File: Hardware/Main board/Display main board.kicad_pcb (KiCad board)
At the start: 2 copper layers, 142.2 x 91.4 mm, 87 parts, among them J1 Board to Board, J2 BATT JST, J3 Conn_ARM_SWD_TagConnect_TC203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, P1 USB_C_Plug_USB2.0, SW1 USB BOOT, U1 BQ25895, U10 ABM8-272-T3, U2 W25Q32JVSS, U3 TS3USB221A, U4 AP7361C-33E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

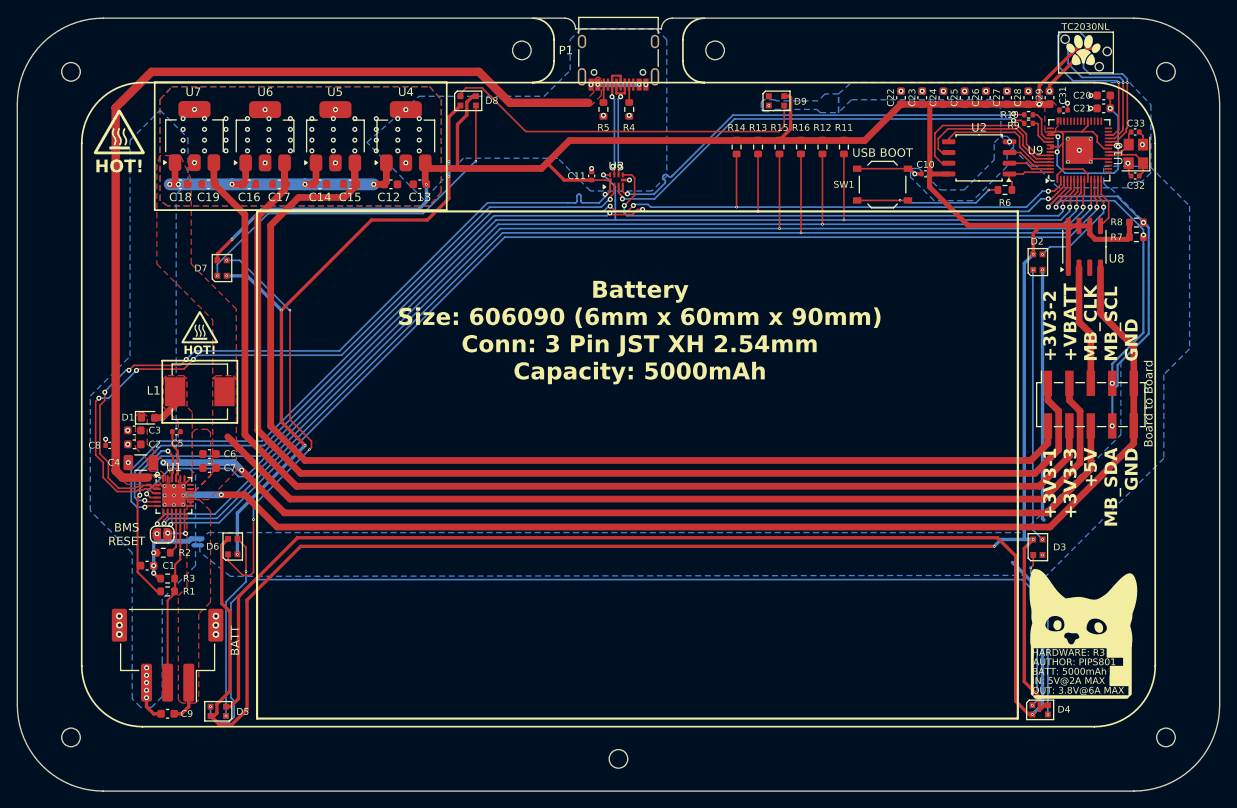
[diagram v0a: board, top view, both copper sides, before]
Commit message: move debug header
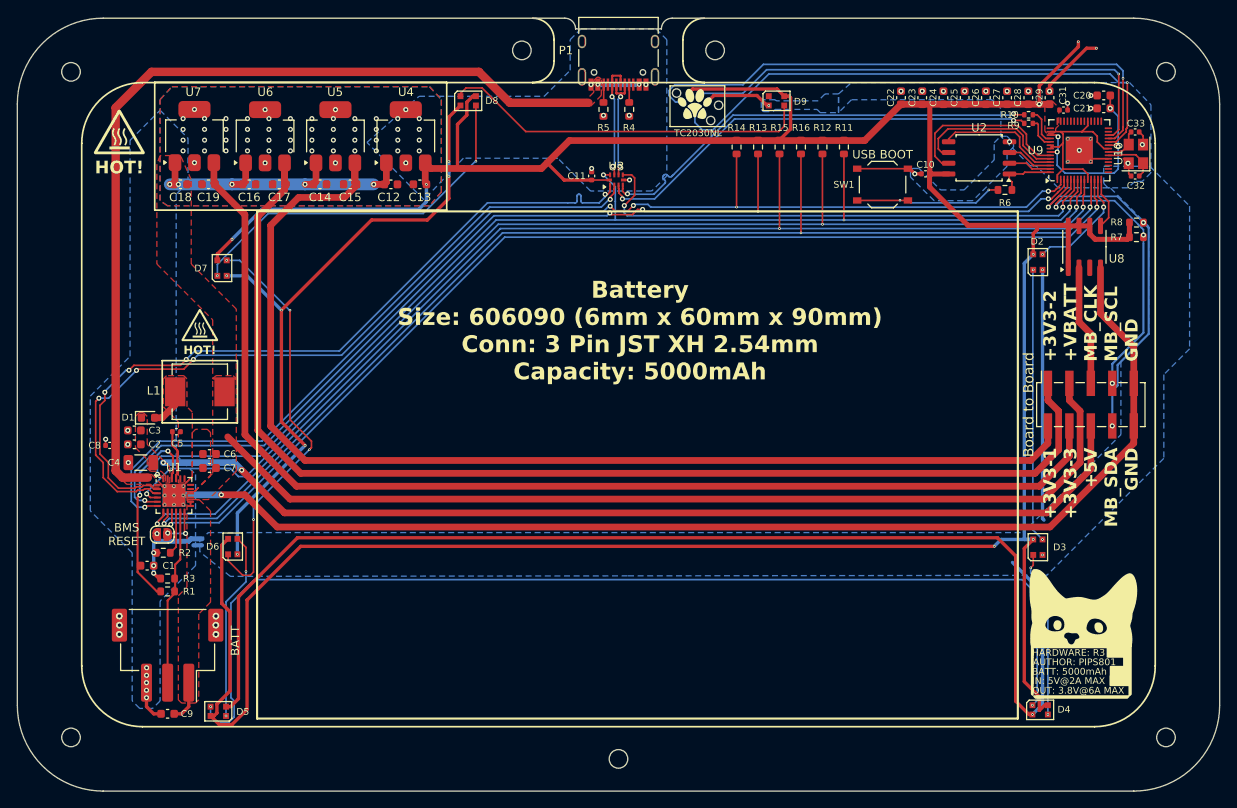
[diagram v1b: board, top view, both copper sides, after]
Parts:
- removed the G*** at (137.3, 96.5)
- moved J3 46.4 mm to (146.5, 61.3)
- moved G** 46.4 mm to (146.2, 60.9)
- moved G*** 0.25 mm to (87.6, 84.5)
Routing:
- net /RP2040/SWDIO: track 17.3 -> 67.0 mm
- net /RP2040/SWCLK: track 15.9 -> 63.9 mm
- net /RP2040/RUN: track 23.0 -> 59.1 mm
- net +3.3V: track 410.5 -> 422.2 mm, vias 7 -> 8
- net AGND: track 295.8 -> 303.8 mm, vias 31 -> 32

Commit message: Silkscreen sectioning
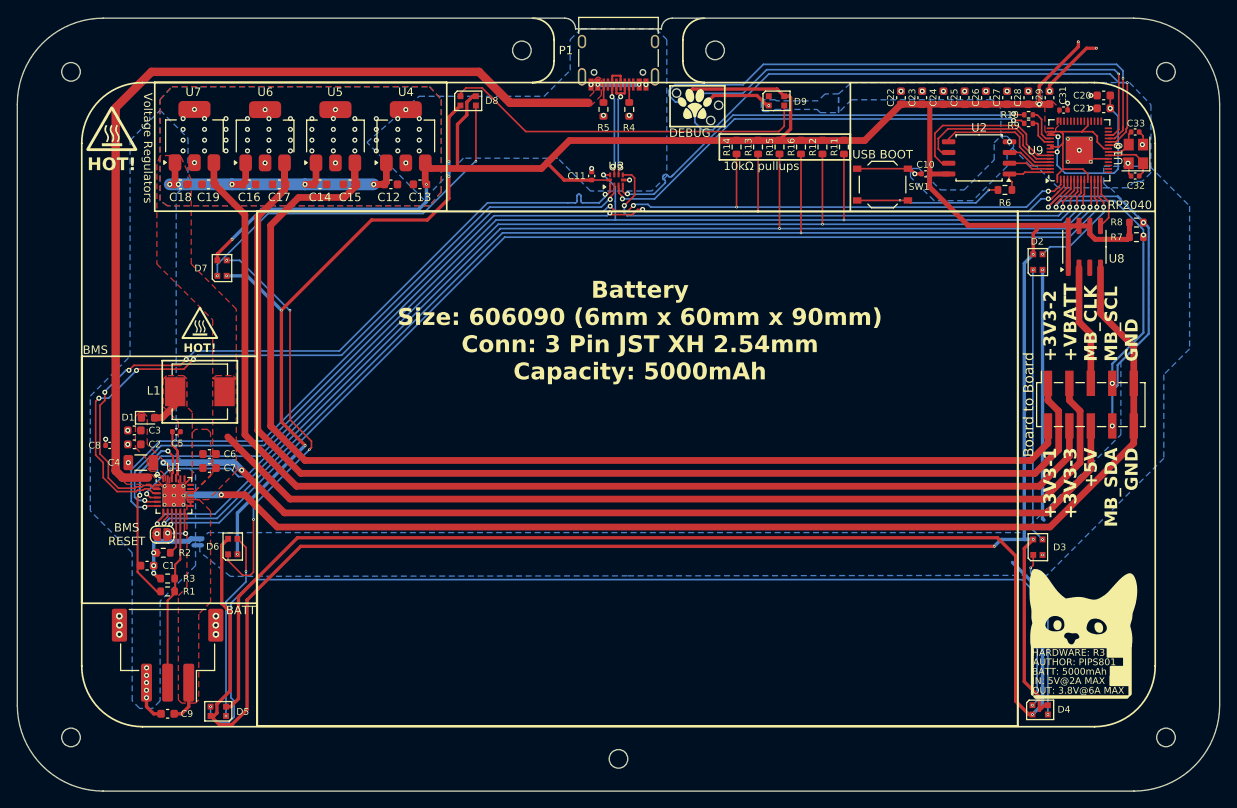
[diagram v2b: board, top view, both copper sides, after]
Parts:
- moved G*** 0.97 mm to (77.2, 61.2)
- moved G*** 0.25 mm to (87.6, 84.2)
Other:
- board text added: "10kΩ pullups"
- board text added: "BMS"
- board text added: "RP2040"
- board text added: "Voltage Regulators"
- board text removed: "TC2030NL"
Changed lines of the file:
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@@
 		(tags "resistor")
 		(property "Reference" "R13"
-			(at -2.286 0 180)
+			(at 0 1.143 -90)
 			(layer "F.SilkS")
 			(effects
@@
 		(tags "resistor")
 		(property "Reference" "R11"
-			(at -2.286 0 0)
+			(at 0 1.143 90)
 			(layer "F.SilkS")
 			(effects
@@
 		(tags "resistor")
 		(property "Reference" "R12"
-			(at -2.286 0 180)
+			(at 0 1.143 -90)
 			(layer "F.SilkS")
 			(effects
@@
 	(footprint "LOGO"
 		(layer "F.Cu")
-		(at 87.630001 84.464661)
+		(at 87.630001 84.210661)
 		(property "Reference" "G***"
 			(at 0 0 0)
@@
 		(tags "resistor")
 		(property "Reference" "R15"
-			(at -2.286 0 180)
+			(at 0 1.143 -90)
 			(layer "F.SilkS")
 			(effects
@@
 		(tags "resistor")
 		(property "Reference" "R16"
-			(at -2.286 0 180)
+			(at 0 1.143 -90)
 			(layer "F.SilkS")
 			(effects
@@
 		(tags "resistor")
 		(property "Reference" "R14"
-			(at -2.286 0 180)
+			(at 0 1.143 -90)
 			(layer "F.SilkS")
 			(effects
@@
 		(tags "SPST Tactile Switch")
 		(property "Reference" "SW1"
-			(at 4.572 0 360)
+			(at -4.318 -0.254 360)
 			(layer "F.SilkS")
 			(effects
@@
 	(footprint "LOGO"
 		(layer "F.Cu")
-		(at 78.105001 61.616062)
+		(at 77.216001 61.235062)
 		(property "Reference" "G***"
 			(at 0 0 0)
@@
 	(gr_rect
 		(start 82.296 58.395)
-		(end 116.84 73.508)
+		(end 116.84 73.635)
 		(stroke
 			(width 0.2)
@@
 		(layer "F.SilkS")
 	)
+	(gr_line
+		(start 184.404 73.66)
+		(end 200.66 73.66)
+		(stroke
+			(width 0.2)
+			(type default)
+		)
+		(layer "F.SilkS")
+	)
 	(gr_arc
 		(start 80.844 134.62)
@@
 		(layer "F.SilkS")
 	)
+	(gr_rect
+		(start 73.66 90.805)
+		(end 94.361 120.015)
+		(stroke
+			(width 0.2)
+			(type default)
+		)
+		(fill none)
+		(layer "F.SilkS")
+	)
 	(gr_line
 		(start 193.476 134.62)
@@
 		(end 149.733 63.627)
 		(stroke
-			(width 0.15)
+			(width 0.2)
 			(type default)
 		)
@@
 	(gr_rect
 		(start 94.404 73.66)
-		(end 184.404 133.66)
+		(end 184.404 134.549)
 		(stroke
 			(width 0.25)
@@
 	)
 	(gr_line
+		(start 200.66 73.66)
+		(end 200.66 65.604)
+		(stroke
+			(width 0.1)
+			(type default)
+		)
+		(layer "F.SilkS")
+	)
+	(gr_line
 		(start 144.78 53.34)
 		(end 144.78 55.88)
@@
 		(layer "F.SilkS")
 	)
+	(gr_rect
+		(start 149.098 64.516)
+		(end 164.592 67.564)
+		(stroke
+			(width 0.2)
+			(type default)
+		)
+		(fill none)
+		(layer "F.SilkS")
+	)
 	(gr_arc
 		(start 200.66 127.436)
@@
 		(layer "F.SilkS")
 	)
+	(gr_line
+		(start 164.592 73.66)
+		(end 164.592 58.42)
+		(stroke
+			(width 0.2)
+			(type default)
+		)
+		(layer "F.SilkS")
+	)
 	(gr_rect
 		(start 94.404 73.66)
@@
 		)
 	)
+	(gr_text "10kΩ pullups"
+		(at 154.06662 68.885664 0)
+		(layer "F.SilkS" knockout)
+		(effects
+			(font
+				(size 1 1)
+				(thickness 0.2)
+			)
+			(justify bottom)
+		)
+	)
 	(gr_text "BATT: 5000mAh"
 		(at 186.067629 128.566566 0)
@@
 	)
 	(gr_text "BATT\n"
-		(at 91.821 126.238 90)
-		(layer "F.SilkS")
+		(at 90.715641 120.8507 0)
+		(layer "F.SilkS" knockout)
 		(effects
 			(font
 				(size 1 1)
-				(thickness 0.15)
+				(thickness 0.2)
 			)
 			(justify left)
@@
 		)
 	)
-	(gr_text "TC2030NL"
-		(at 146.558 64.389 -0)
-		(layer "F.SilkS")
+	(gr_text "DEBUG"
+		(at 145.597381 64.380029 -0)
+		(layer "F.SilkS" knockout)
 		(effects
 			(font
-				(size 0.8 0.8)
-				(thickness 0.15)
+				(size 1 1)
+				(thickness 0.2)
+			)
+		)
+	)
+	(gr_text "RP2040"
+		(at 197.649945 73.492659 0)
+		(layer "F.SilkS" knockout)
+		(effects
+			(font
+				(size 1 1)
+				(thickness 0.2)
+			)
+			(justify bottom)
+		)
+	)
+	(gr_text "BMS"
+		(at 75.267646 90.637849 0)
+		(layer "F.SilkS" knockout)
+		(effects
+			(font
+				(size 1 1)
+				(thickness 0.2)
 			)
+			(justify bottom)
 		)
 	)
@@
 		)
 	)
+	(gr_text "Voltage Regulators"
+		(at 80.899 66.167 -90)
+		(layer "F.SilkS" knockout)
+		(effects
+			(font
+				(size 1 1)
+				(thickness 0.2)
+			)
+			(justify bottom)
+		)
+	)
 	(gr_text "OUT: 3.8V@6A MAX"
 		(at 186.10673 130.81 0)
@@
 	)
 	(gr_text "HOT!"
-		(at 78.105 69.342 0)
+		(at 77.216 68.961 0)
 		(layer "F.SilkS")
 		(effects
@@
 	)
 	(gr_text "HOT!"
-		(at 87.63 90.6566 0)
+		(at 87.63 90.4026 0)
 		(layer "F.SilkS")
 		(effects

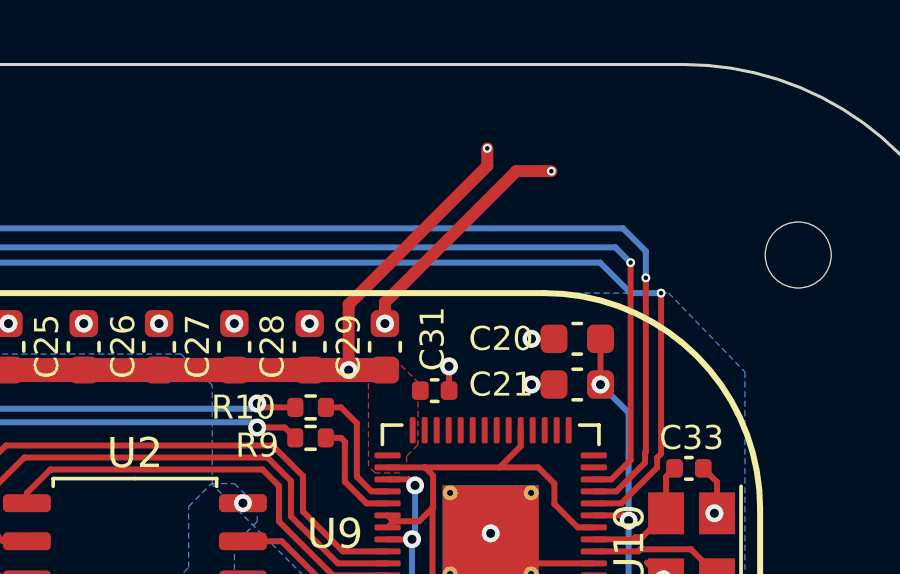
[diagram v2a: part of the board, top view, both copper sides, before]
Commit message: remove unused traces
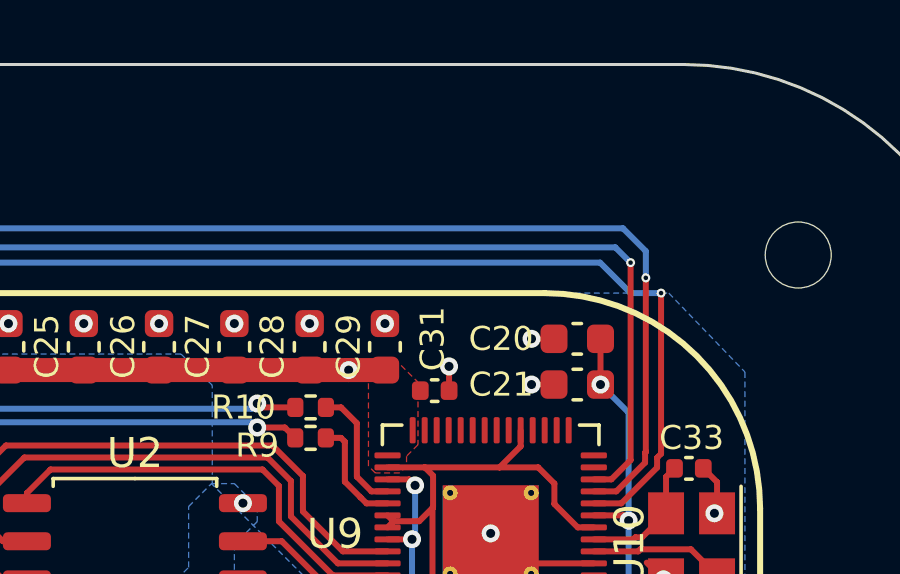
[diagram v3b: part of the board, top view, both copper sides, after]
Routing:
- net +3.3V: track 422.2 -> 412.9 mm, vias 8 -> 7
- net AGND: track 303.8 -> 295.8 mm, vias 32 -> 31
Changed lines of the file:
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@@
-	)
-	(segment
-		(start 191.5668 54.1782)
-		(end 191.5668 53.594)
-		(width 0.4)
-		(layer "F.Cu")
-		(net 13)
 	)
 	(segment
@@
 	)
 	(segment
-		(start 186.944 58.801)
-		(end 191.5668 54.1782)
-		(width 0.4)
-		(layer "F.Cu")
-		(net 13)
-	)
-	(segment
 		(start 192.913 76.327)
 		(end 193.548 76.962)
@@
 	)
 	(segment
-		(start 186.944 60.986)
-		(end 186.944 58.801)
-		(width 0.4)
-		(layer "F.Cu")
-		(net 13)
-	)
-	(segment
 		(start 192.678 69.234)
 		(end 192.678 69.867)
@@
 		(size 0.6)
 		(drill 0.3)
-		(layers "F.Cu" "B.Cu")
-		(net 13)
-	)
-	(via
-		(at 191.5668 53.594)
-		(size 0.3)
-		(drill 0.15)
 		(layers "F.Cu" "B.Cu")
 		(net 13)
@@
 	)
 	(segment
-		(start 188.154 58.734)
-		(end 192.532 54.356)
-		(width 0.4)
-		(layer "F.Cu")
-		(net 19)
-	)
-	(segment
 		(start 153.543 59.944)
 		(end 148.450678 59.944)
@@
 	)
 	(segment
-		(start 188.154 59.436)
-		(end 188.154 58.734)
-		(width 0.4)
-		(layer "F.Cu")
-		(net 19)
-	)
-	(segment
 		(start 97.282 98.552)
 		(end 100.076 101.346)
@@
 		(start 173.002 69.215)
 		(end 172.212 69.215)
-		(width 0.4)
-		(layer "F.Cu")
-		(net 19)
-	)
-	(segment
-		(start 192.532 54.356)
-		(end 193.7004 54.356)
 		(width 0.4)
 		(layer "F.Cu")
@@
 		(layers "F.Cu" "B.Cu")
 		(net 19)
-	)
-	(via
-		(at 193.7004 54.356)
-		(size 0.3)
-		(drill 0.15)
-		(layers "F.Cu" "B.Cu")
-		(net 19)

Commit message: update constraints
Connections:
- D2 pad 3: Net-(D2-DIN) -> unconnected-(D2-DIN-Pad3)
- U9 pad 13: Net-(D2-DIN) -> unconnected-(U9-GPIO10-Pad13)
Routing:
- net Net-(D2-DIN): track 13.5 -> 0.00 mm, vias 2 -> 0
- net (no net): track 0.00 -> 13.5 mm, vias 6 -> 8

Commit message: fix nets
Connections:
- D2 pad 3: unconnected-(D2-DIN-Pad3) -> Net-(D2-DIN)
- U9 pad 13: unconnected-(U9-GPIO10-Pad13) -> Net-(D2-DIN)
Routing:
- net Net-(D2-DIN): track 0.00 -> 13.5 mm, vias 0 -> 2
- net (no net): track 13.5 -> 0.00 mm, vias 8 -> 6

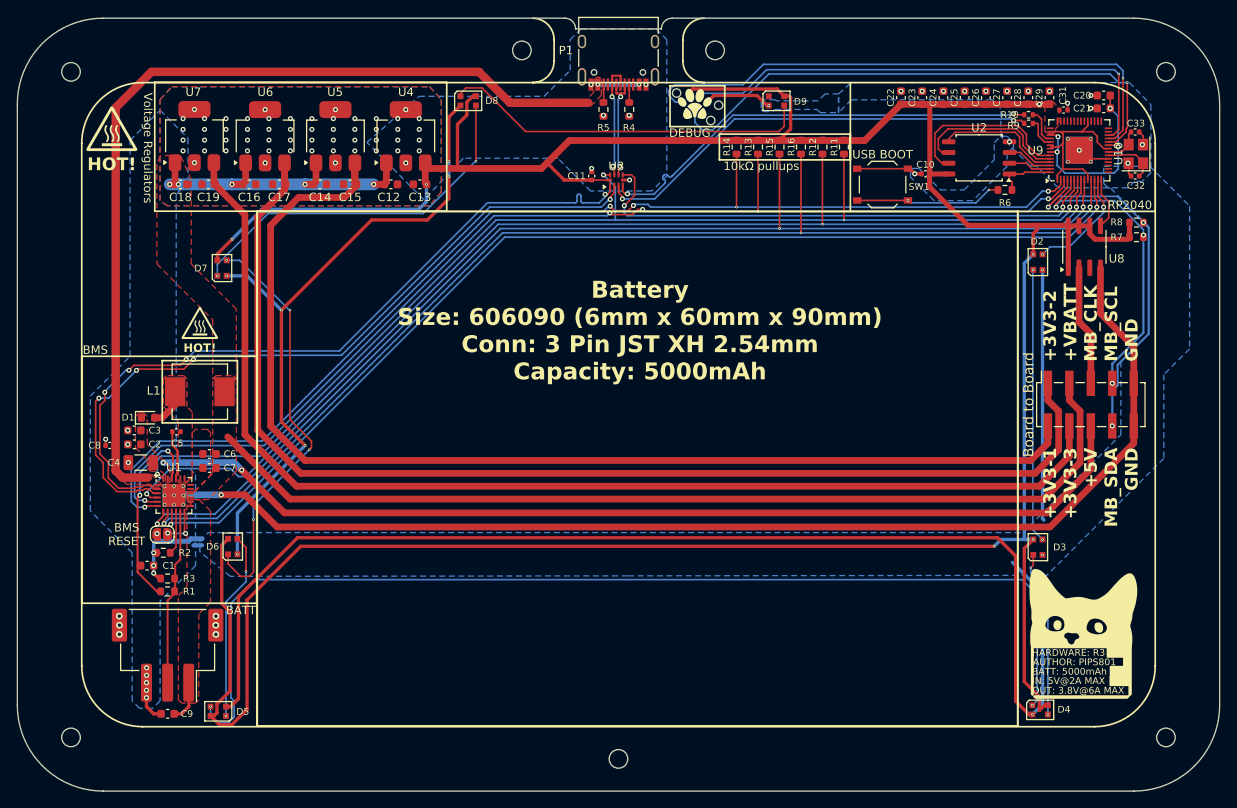
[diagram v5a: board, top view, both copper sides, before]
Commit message: add caps for LEDs
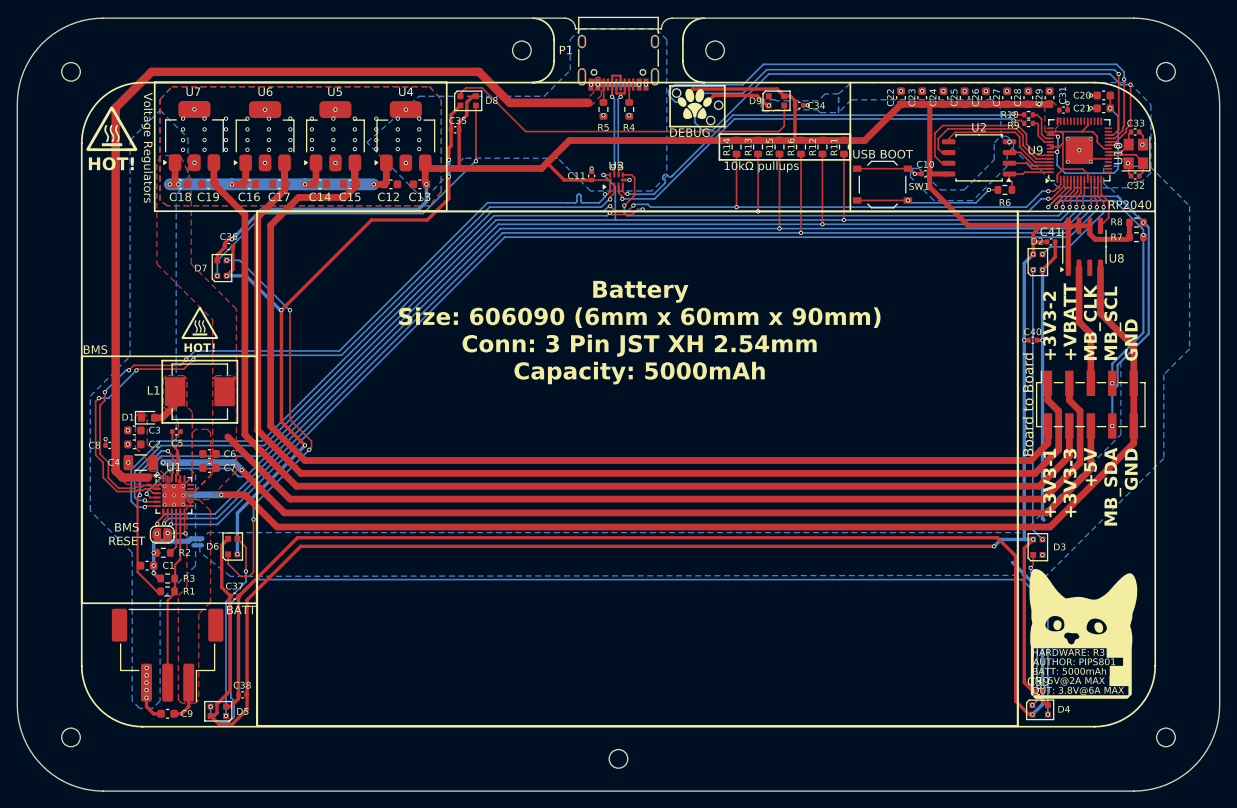
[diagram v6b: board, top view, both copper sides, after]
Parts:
- added C34: 0.1μF, Capacitor_SMD:C_0402_1005Metric, F.Cu at (158.5, 61.1)
- added C35: 0.1μF, Capacitor_SMD:C_0402_1005Metric, F.Cu at (117.8, 64.0)
- added C36: 0.1μF, Capacitor_SMD:C_0402_1005Metric, F.Cu at (91.1, 77.8)
- added C37: 0.1μF, Capacitor_SMD:C_0402_1005Metric, F.Cu at (91.7, 119.2)
- added C38: 0.1μF, Capacitor_SMD:C_0402_1005Metric, F.Cu at (92.7, 130.9)
- added C39: 0.1μF, Capacitor_SMD:C_0402_1005Metric, F.Cu at (186.8, 130.5)
- added C40: 0.1μF, Capacitor_SMD:C_0402_1005Metric, F.Cu at (186.2, 88.9)
- added C41: 0.1μF, Capacitor_SMD:C_0402_1005Metric, F.Cu at (188.3, 77.3)
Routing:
- net AGND: track 295.8 -> 305.2 mm, vias 31 -> 34
- net +3.3V: track 412.9 -> 415.2 mm, vias 7 -> 8
- net (no net): vias 6 -> 0
